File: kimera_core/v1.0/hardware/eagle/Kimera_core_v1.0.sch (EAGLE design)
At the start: 24 parts, among them IC1 PCA9555RGER-NOPAD, IC2 PCA9555RGER-NOPAD, U1 ATMEGA32U4QFN2, Y1 CSTCR6M00G53Z

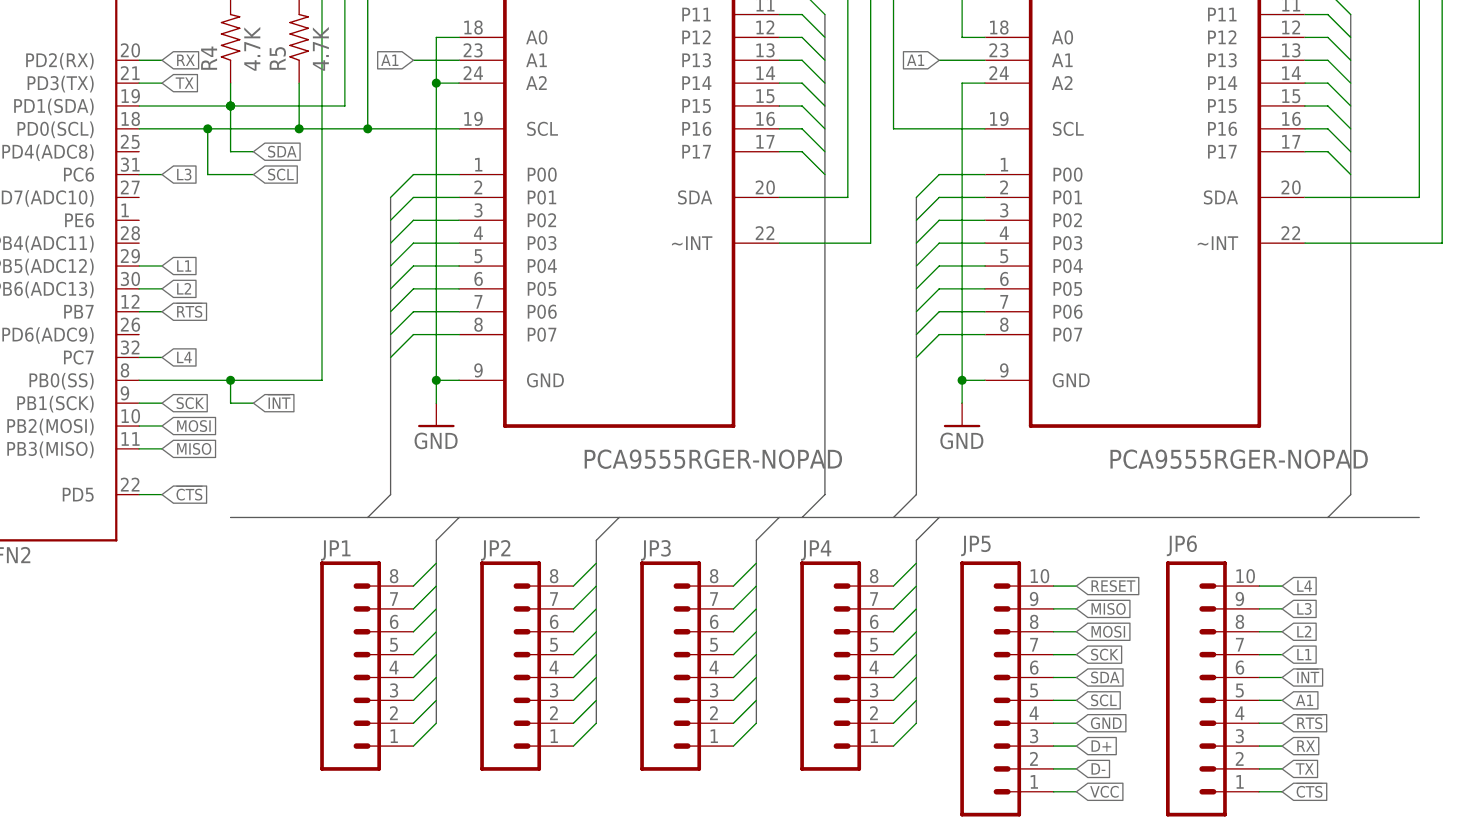
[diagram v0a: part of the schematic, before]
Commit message: kimera_core: Change signal name of LED pins
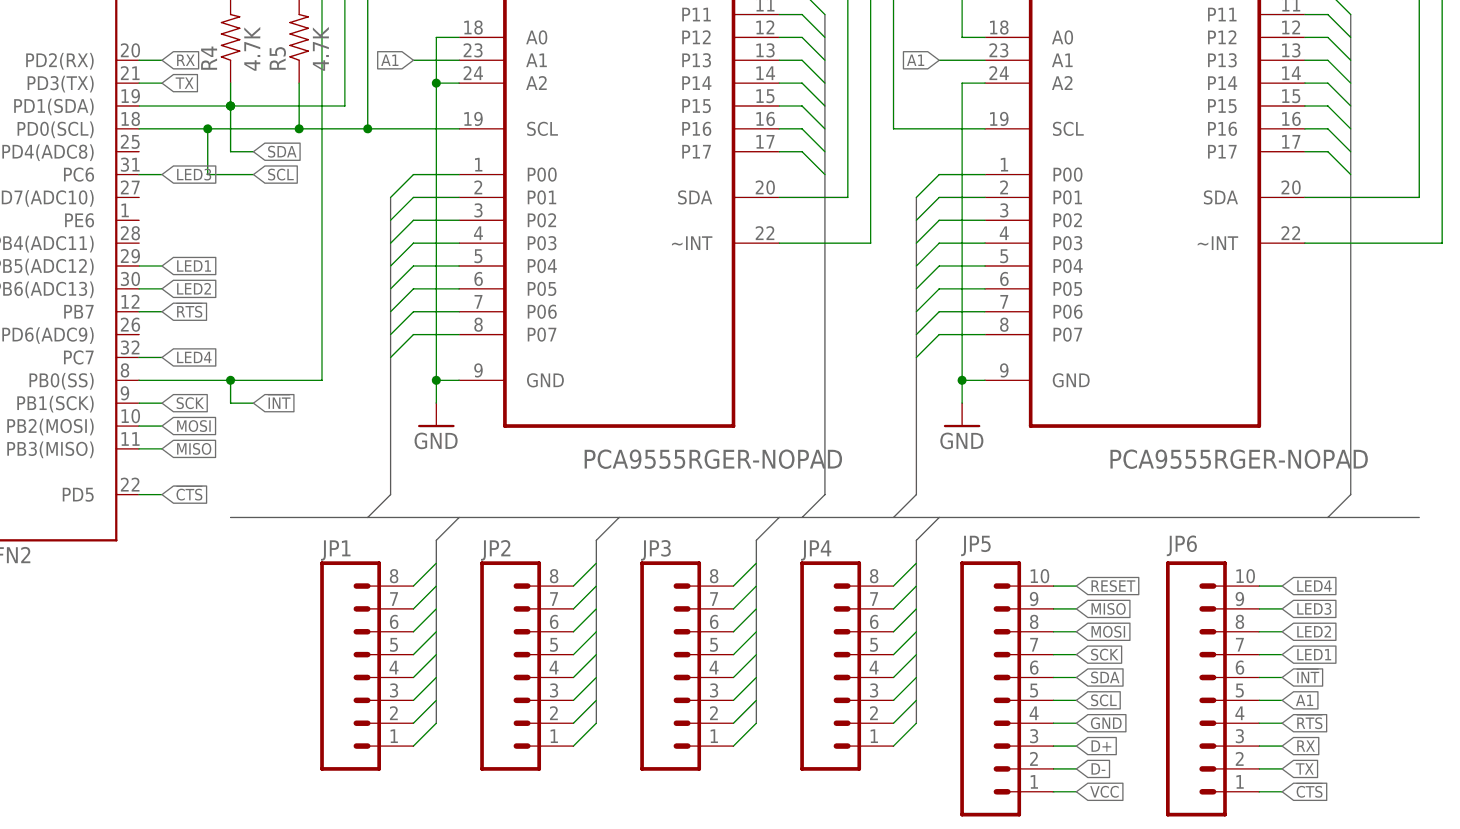
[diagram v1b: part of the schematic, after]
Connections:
- net L1 renamed LED1
- net L2 renamed LED2
- net L3 renamed LED3
- net L4 renamed LED4
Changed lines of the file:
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@@
 </segment>
 </net>
-<net name="L2" class="0">
+<net name="LED2" class="0">
 <segment>
 <pinref part="JP6" gate="G$1" pin="8"/>
@@
 </segment>
 </net>
-<net name="L1" class="0">
-<segment>
-<pinref part="JP6" gate="G$1" pin="7"/>
-<wire x1="228.6" y1="53.34" x2="231.14" y2="53.34" width="0.1524" layer="91"/>
-<label x="231.14" y="53.34" size="1.27" layer="95" xref="yes"/>
-</segment>
-<segment>
-<pinref part="U1" gate="G$1" pin="PB5(ADC12)"/>
-<wire x1="104.14" y1="96.52" x2="106.68" y2="96.52" width="0.1524" layer="91"/>
-<label x="106.68" y="96.52" size="1.27" layer="95" xref="yes"/>
-</segment>
-</net>
-<net name="L3" class="0">
+<net name="LED3" class="0">
 <segment>
 <pinref part="JP6" gate="G$1" pin="9"/>
@@
 </segment>
 </net>
-<net name="L4" class="0">
+<net name="LED4" class="0">
 <segment>
 <pinref part="JP6" gate="G$1" pin="10"/>
@@
 </segment>
 </net>
+<net name="LED1" class="0">
+<segment>
+<pinref part="JP6" gate="G$1" pin="7"/>
+<wire x1="228.6" y1="53.34" x2="231.14" y2="53.34" width="0.1524" layer="91"/>
+<label x="231.14" y="53.34" size="1.27" layer="95" xref="yes"/>
+</segment>
+<segment>
+<pinref part="U1" gate="G$1" pin="PB5(ADC12)"/>
+<wire x1="104.14" y1="96.52" x2="106.68" y2="96.52" width="0.1524" layer="91"/>
+<label x="106.68" y="96.52" size="1.27" layer="95" xref="yes"/>
+</segment>
+</net>
